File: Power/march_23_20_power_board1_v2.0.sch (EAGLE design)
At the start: 58 parts, among them J0_PLOAD_CONN 172648-0102, J1_B3_CONN 105313-1102, J2_LORA_CONN 105313-1102, J3_SPOT_CONN 105313-1102, J4_SSSBOARD_CONN 172648-0102, Q1 FQD11P06TM

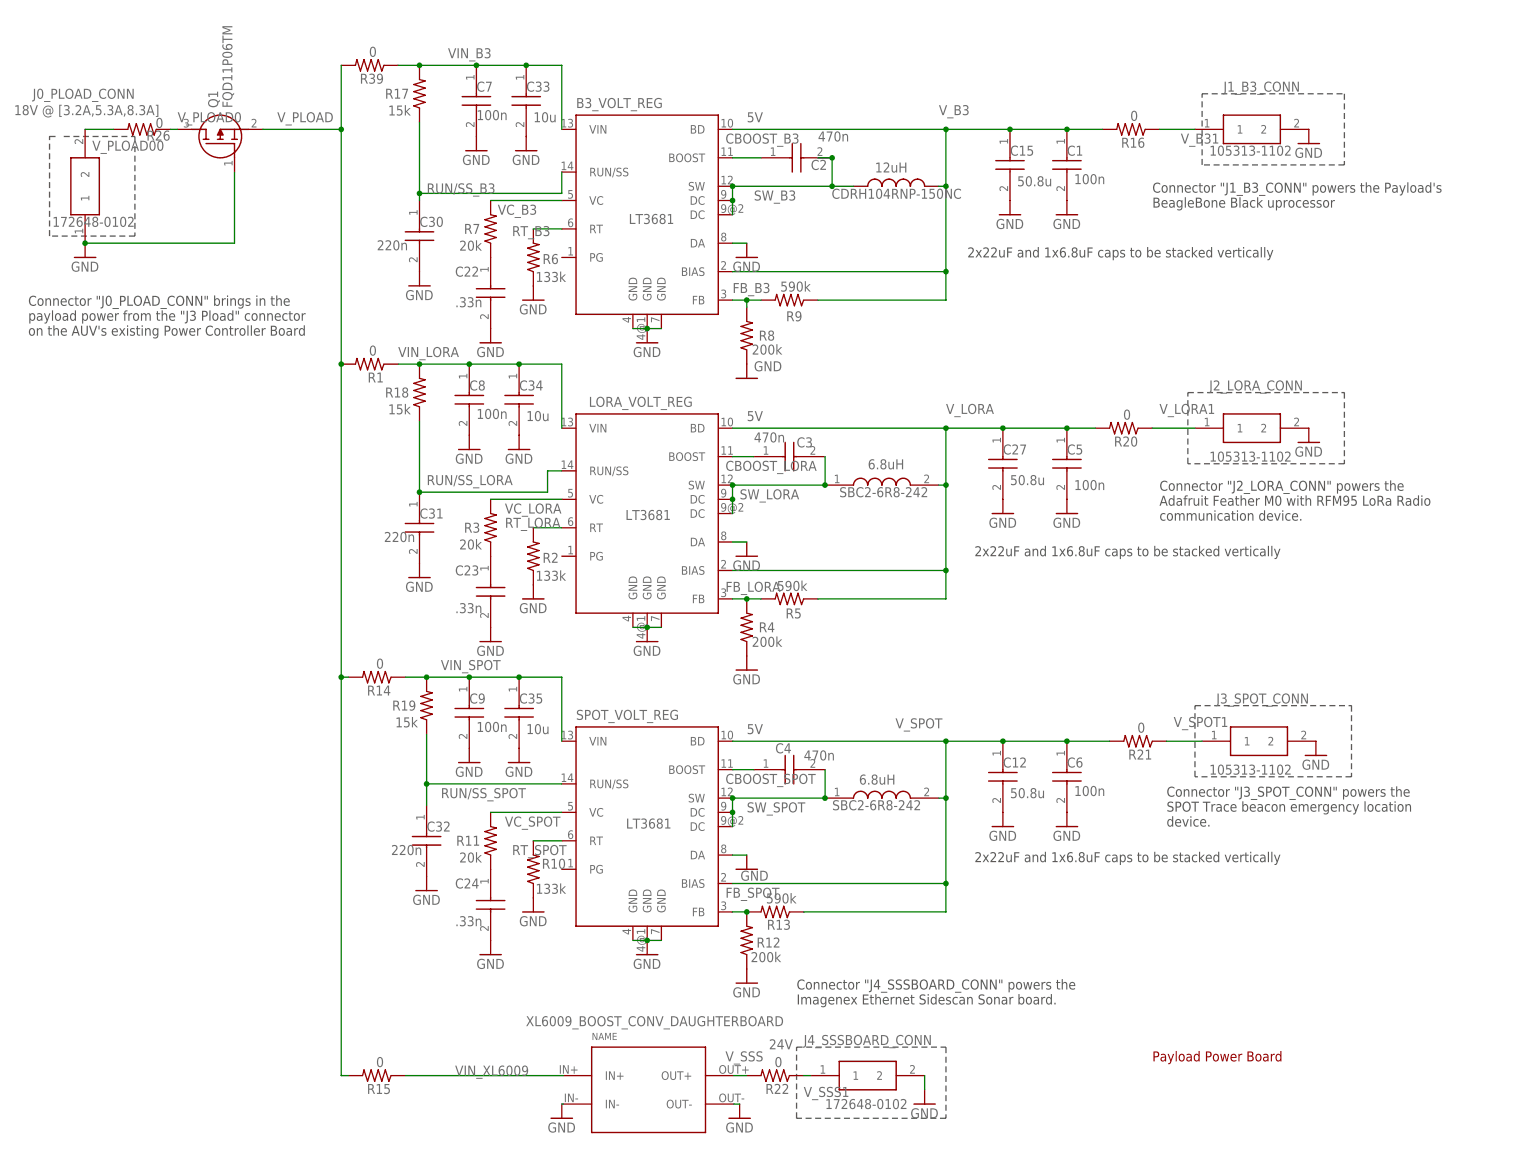
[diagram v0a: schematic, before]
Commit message: Cleaned up the Payload Power Board sch and brd and am almost done with the Voltage Lines Board sch and brd
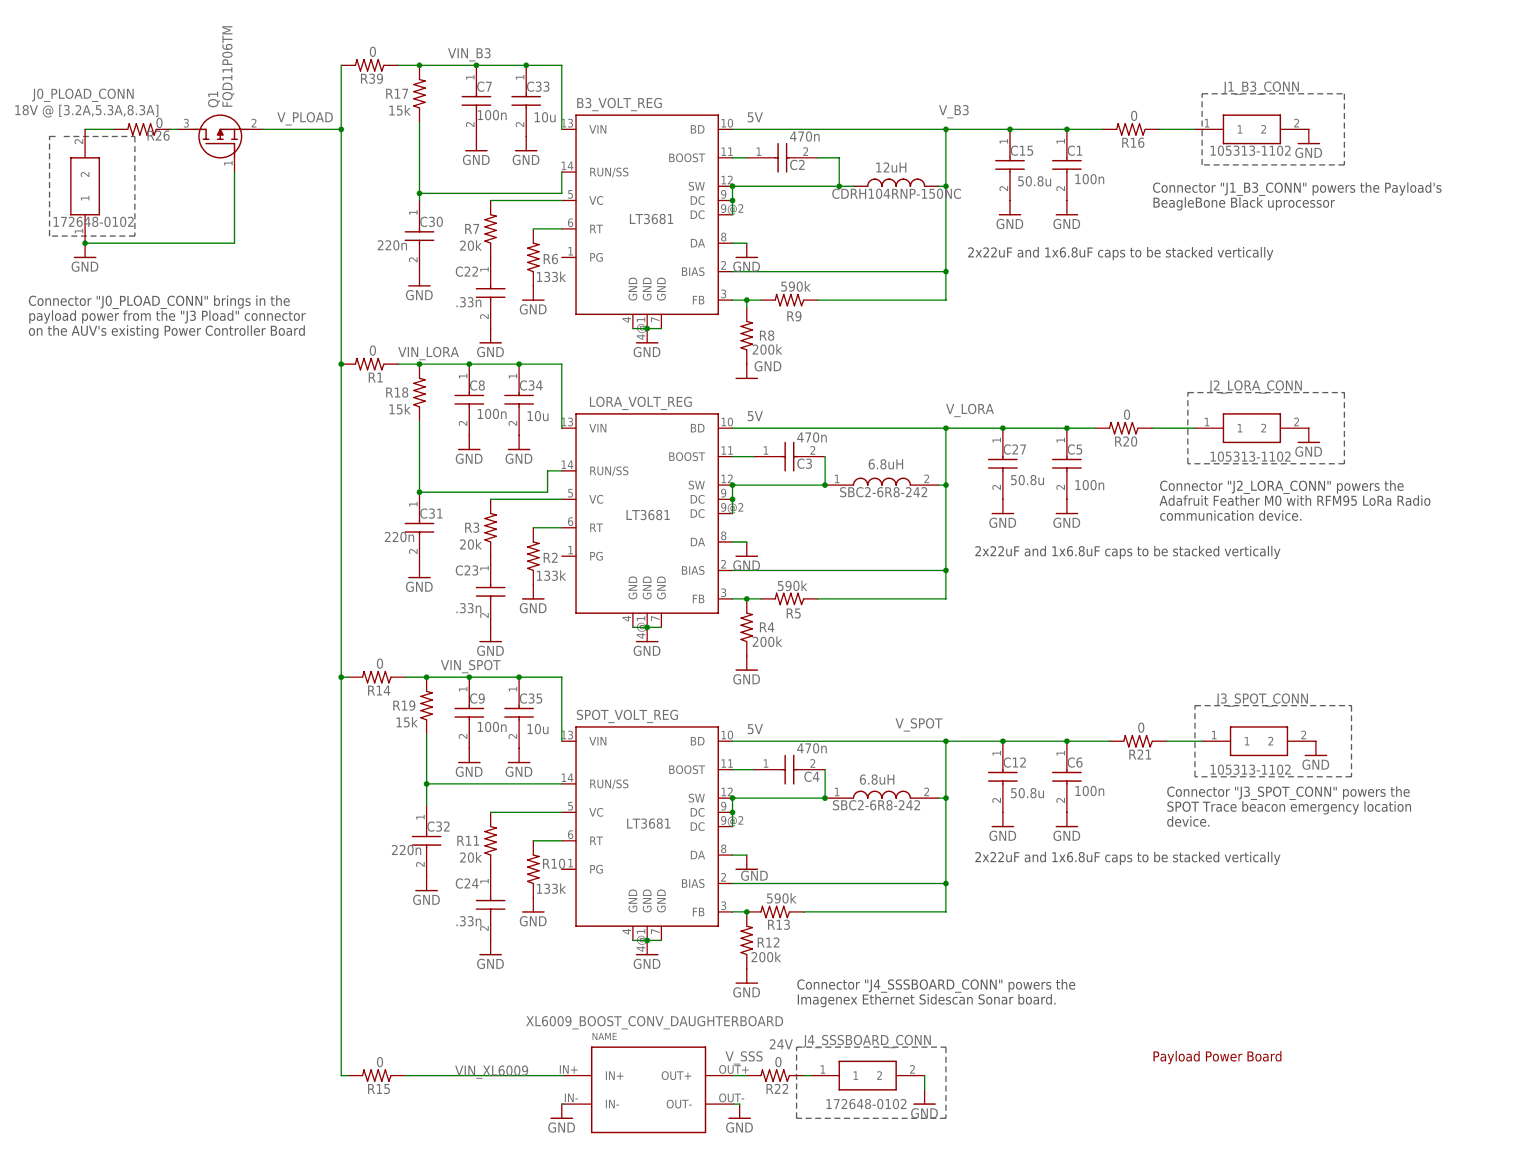
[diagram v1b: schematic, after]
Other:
- moved on the sheet: C2
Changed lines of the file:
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@@
 <setting verticaltext="up"/>
 </settings>
-<grid distance="50" unitdist="mil" unit="mil" style="lines" multiple="1" display="yes" altdistance="0.01" altunitdist="inch" altunit="mil"/>
+<grid distance="0.1" unitdist="inch" unit="inch" style="lines" multiple="1" display="no" altdistance="0.01" altunitdist="inch" altunit="inch"/>
 <layers>
 <layer number="1" name="Top" color="4" fill="1" visible="no" active="no"/>
@@
 <text x="195.58" y="231.14" size="1.778" layer="96">10u</text>
 <text x="196.85" y="284.48" size="1.778" layer="96">10u</text>
-<text x="236.22" y="227.33" size="1.778" layer="96">470n</text>
+<text x="243.84" y="227.33" size="1.778" layer="96">470n</text>
 <text x="283.21" y="273.05" size="1.778" layer="96">50.8u</text>
 <text x="281.94" y="219.71" size="1.778" layer="96">50.8u</text>
@@
 <attribute name="VALUE" x="279.4" y="265.43" size="1.778" layer="96"/>
 </instance>
-<instance part="C2" gate="G$1" x="237.49" y="278.13" smashed="yes">
-<attribute name="NAME" x="246.38" y="276.86" size="1.778" layer="95" align="center-left"/>
-<attribute name="VALUE" x="247.65" y="281.94" size="1.778" layer="96" align="center-left"/>
+<instance part="C2" gate="G$1" x="234.95" y="278.13" smashed="yes">
+<attribute name="NAME" x="242.57" y="276.86" size="1.778" layer="95" align="center-left"/>
+<attribute name="VALUE" x="242.57" y="281.94" size="1.778" layer="96" align="center-left"/>
 </instance>
 <instance part="C3" gate="G$1" x="236.22" y="224.79" smashed="yes">
-<attribute name="NAME" x="243.84" y="227.33" size="1.778" layer="95" align="center-left"/>
+<attribute name="NAME" x="243.84" y="223.52" size="1.778" layer="95" align="center-left"/>
 </instance>
 <instance part="C4" gate="G$1" x="236.22" y="168.91" smashed="yes">
-<attribute name="NAME" x="240.03" y="172.72" size="1.778" layer="95" align="center-left"/>
-<attribute name="VALUE" x="245.11" y="171.45" size="1.778" layer="96" align="center-left"/>
+<attribute name="NAME" x="245.11" y="167.64" size="1.778" layer="95" align="center-left"/>
+<attribute name="VALUE" x="243.84" y="172.72" size="1.778" layer="96" align="center-left"/>
 </instance>
 <instance part="C1" gate="G$1" x="292.1" y="283.21" smashed="yes" rot="R270">
@@
 <wire x1="232.41" y1="143.51" x2="234.95" y2="143.51" width="0.1524" layer="91"/>
 <junction x="234.95" y="143.51"/>
-<label x="231.14" y="146.05" size="1.778" layer="95"/>
 </segment>
 </net>
@@
 <pinref part="B3_VOLT_REG" gate="G$1" pin="RT"/>
 <wire x1="196.85" y1="265.43" x2="201.93" y2="265.43" width="0.1524" layer="91"/>
-<label x="193.04" y="264.16" size="1.778" layer="95"/>
 </segment>
 </net>
@@
 <wire x1="201.93" y1="271.78" x2="176.53" y2="271.78" width="0.1524" layer="91"/>
 <junction x="176.53" y="271.78"/>
-<label x="177.8" y="271.78" size="1.778" layer="95"/>
 <pinref part="C30" gate="G$1" pin="1"/>
 </segment>
@@
 <pinref part="B3_VOLT_REG" gate="G$1" pin="VC"/>
 <wire x1="189.23" y1="270.51" x2="201.93" y2="270.51" width="0.1524" layer="91"/>
-<label x="190.5" y="267.97" size="1.778" layer="95"/>
 </segment>
 </net>
@@
 <segment>
 <pinref part="B3_VOLT_REG" gate="G$1" pin="BOOST"/>
-<wire x1="232.41" y1="278.13" x2="237.49" y2="278.13" width="0.1524" layer="91"/>
-<label x="231.14" y="280.67" size="1.778" layer="95"/>
+<wire x1="232.41" y1="278.13" x2="234.95" y2="278.13" width="0.1524" layer="91"/>
 <pinref part="C2" gate="G$1" pin="1"/>
 </segment>
@@
 <wire x1="234.95" y1="251.46" x2="234.95" y2="252.73" width="0.1524" layer="91"/>
 <junction x="234.95" y="252.73"/>
-<label x="232.41" y="254" size="1.778" layer="95"/>
 </segment>
 </net>
@@
 <pinref part="SPOT_VOLT_REG" gate="G$1" pin="RT"/>
 <wire x1="196.85" y1="156.21" x2="201.93" y2="156.21" width="0.1524" layer="91"/>
-<label x="193.04" y="153.67" size="1.778" layer="95"/>
 </segment>
 </net>
@@
 <pinref part="SPOT_VOLT_REG" gate="G$1" pin="VC"/>
 <wire x1="189.23" y1="161.29" x2="201.93" y2="161.29" width="0.1524" layer="91"/>
-<label x="191.77" y="158.75" size="1.778" layer="96"/>
 </segment>
 </net>
@@
 <pinref part="R19" gate="G$1" pin="1"/>
 <wire x1="177.8" y1="175.26" x2="177.8" y2="166.37" width="0.1524" layer="91"/>
-<label x="180.34" y="163.83" size="1.778" layer="95"/>
 <pinref part="C32" gate="G$1" pin="1"/>
 <junction x="177.8" y="166.37"/>
@@
 <wire x1="199.39" y1="222.25" x2="199.39" y2="218.44" width="0.1524" layer="91"/>
 <wire x1="199.39" y1="218.44" x2="176.53" y2="218.44" width="0.1524" layer="91"/>
-<label x="177.8" y="219.71" size="1.778" layer="95"/>
 <pinref part="C31" gate="G$1" pin="1"/>
 <junction x="176.53" y="218.44"/>
@@
 <pinref part="LORA_VOLT_REG" gate="G$1" pin="VC"/>
 <wire x1="189.23" y1="217.17" x2="201.93" y2="217.17" width="0.1524" layer="91"/>
-<label x="191.77" y="214.63" size="1.778" layer="95"/>
 </segment>
 </net>
@@
 <pinref part="LORA_VOLT_REG" gate="G$1" pin="RT"/>
 <wire x1="196.85" y1="212.09" x2="201.93" y2="212.09" width="0.1524" layer="91"/>
-<label x="191.77" y="212.09" size="1.778" layer="95"/>
 </segment>
 </net>
@@
 <wire x1="234.95" y1="199.39" x2="237.49" y2="199.39" width="0.1524" layer="91"/>
 <junction x="234.95" y="199.39"/>
-<label x="231.14" y="200.66" size="1.778" layer="95"/>
 </segment>
 </net>
@@
 <pinref part="LORA_VOLT_REG" gate="G$1" pin="BOOST"/>
 <wire x1="232.41" y1="224.79" x2="236.22" y2="224.79" width="0.1524" layer="91"/>
-<label x="231.14" y="222.25" size="1.778" layer="95"/>
 <pinref part="C3" gate="G$1" pin="1"/>
 </segment>
@@
 <wire x1="232.41" y1="163.83" x2="248.92" y2="163.83" width="0.1524" layer="91"/>
 <junction x="232.41" y="163.83"/>
-<label x="234.95" y="161.29" size="1.778" layer="95"/>
 <wire x1="248.92" y1="163.83" x2="248.92" y2="168.91" width="0.1524" layer="91"/>
 <junction x="248.92" y="163.83"/>
@@
 <wire x1="232.41" y1="219.71" x2="248.92" y2="219.71" width="0.1524" layer="91"/>
 <junction x="232.41" y="219.71"/>
-<label x="233.68" y="217.17" size="1.778" layer="95"/>
 <wire x1="248.92" y1="219.71" x2="248.92" y2="224.79" width="0.1524" layer="91"/>
 <junction x="248.92" y="219.71"/>
@@
 <wire x1="232.41" y1="267.97" x2="232.41" y2="270.51" width="0.1524" layer="91"/>
 <pinref part="INDUCTOR_3" gate="G$1" pin="1"/>
-<wire x1="232.41" y1="273.05" x2="250.19" y2="273.05" width="0.1524" layer="91"/>
+<wire x1="232.41" y1="273.05" x2="251.46" y2="273.05" width="0.1524" layer="91"/>
 <junction x="232.41" y="273.05"/>
-<label x="236.22" y="270.51" size="1.778" layer="95"/>
-<wire x1="250.19" y1="273.05" x2="254" y2="273.05" width="0.1524" layer="91"/>
-<wire x1="250.19" y1="278.13" x2="250.19" y2="273.05" width="0.1524" layer="91"/>
-<junction x="250.19" y="273.05"/>
-<wire x1="247.65" y1="278.13" x2="250.19" y2="278.13" width="0.1524" layer="91"/>
 <pinref part="C2" gate="G$1" pin="2"/>
-<junction x="250.19" y="278.13"/>
+<wire x1="251.46" y1="273.05" x2="254" y2="273.05" width="0.1524" layer="91"/>
+<wire x1="247.65" y1="278.13" x2="251.46" y2="278.13" width="0.1524" layer="91"/>
+<wire x1="251.46" y1="278.13" x2="251.46" y2="273.05" width="0.1524" layer="91"/>
+<junction x="251.46" y="273.05"/>
 </segment>
 </net>
@@
 <pinref part="R26" gate="G$1" pin="1"/>
 <wire x1="132.08" y1="283.21" x2="133.35" y2="283.21" width="0.1524" layer="91"/>
-<label x="133.35" y="284.48" size="1.778" layer="95"/>
 <pinref part="Q1" gate="G$1" pin="D"/>
 </segment>
@@
 <wire x1="308.61" y1="283.21" x2="314.96" y2="283.21" width="0.1524" layer="91"/>
 <pinref part="R16" gate="G$1" pin="1"/>
-<label x="312.42" y="280.67" size="1.778" layer="95"/>
 </segment>
 </net>
@@
 <wire x1="307.34" y1="229.87" x2="314.96" y2="229.87" width="0.1524" layer="91"/>
 <pinref part="R20" gate="G$1" pin="1"/>
-<label x="308.61" y="232.41" size="1.778" layer="95"/>
 </segment>
 </net>
@@
 <wire x1="309.88" y1="173.99" x2="316.23" y2="173.99" width="0.1524" layer="91"/>
 <pinref part="R21" gate="G$1" pin="1"/>
-<label x="311.15" y="176.53" size="1.778" layer="95"/>
 </segment>
 </net>
@@
 <pinref part="SPOT_VOLT_REG" gate="G$1" pin="BOOST"/>
 <wire x1="232.41" y1="168.91" x2="236.22" y2="168.91" width="0.1524" layer="91"/>
-<label x="231.14" y="166.37" size="1.778" layer="96"/>
 <pinref part="C4" gate="G$1" pin="1"/>
 </segment>
@@
 <pinref part="R26" gate="G$1" pin="2"/>
 <wire x1="116.84" y1="283.21" x2="121.92" y2="283.21" width="0.1524" layer="91"/>
-<label x="118.11" y="279.4" size="1.778" layer="95"/>
 </segment>
 </net>
@@
 <pinref part="J4_SSSBOARD_CONN" gate="G$1" pin="1"/>
 <wire x1="246.38" y1="114.3" x2="245.11" y2="114.3" width="0.1524" layer="91"/>
-<label x="245.11" y="110.49" size="1.778" layer="95"/>
-</segment>
-</net>
+</segment>
+</net>
